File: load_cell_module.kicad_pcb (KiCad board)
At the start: 2 copper layers, 0 parts

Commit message: Finalized board shape
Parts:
- added H1: MountingScrew, MountingHole:MountingHole_3.2mm_M3, F.Cu at (144.0, 84.0)
- added H2: MountingScrew, MountingHole:MountingHole_3.2mm_M3, F.Cu at (176.0, 84.0)
- added H3: MountingScrew, MountingHole:MountingHole_3.2mm_M3, F.Cu at (144.0, 126.0)
- added H4: MountingScrew, MountingHole:MountingHole_3.2mm_M3, F.Cu at (176.0, 126.0)
- added U1: ~, integral0_lite:integral0_lite, F.Cu at (160.0, 80.7)
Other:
- board outline added: 40 x 50 mm

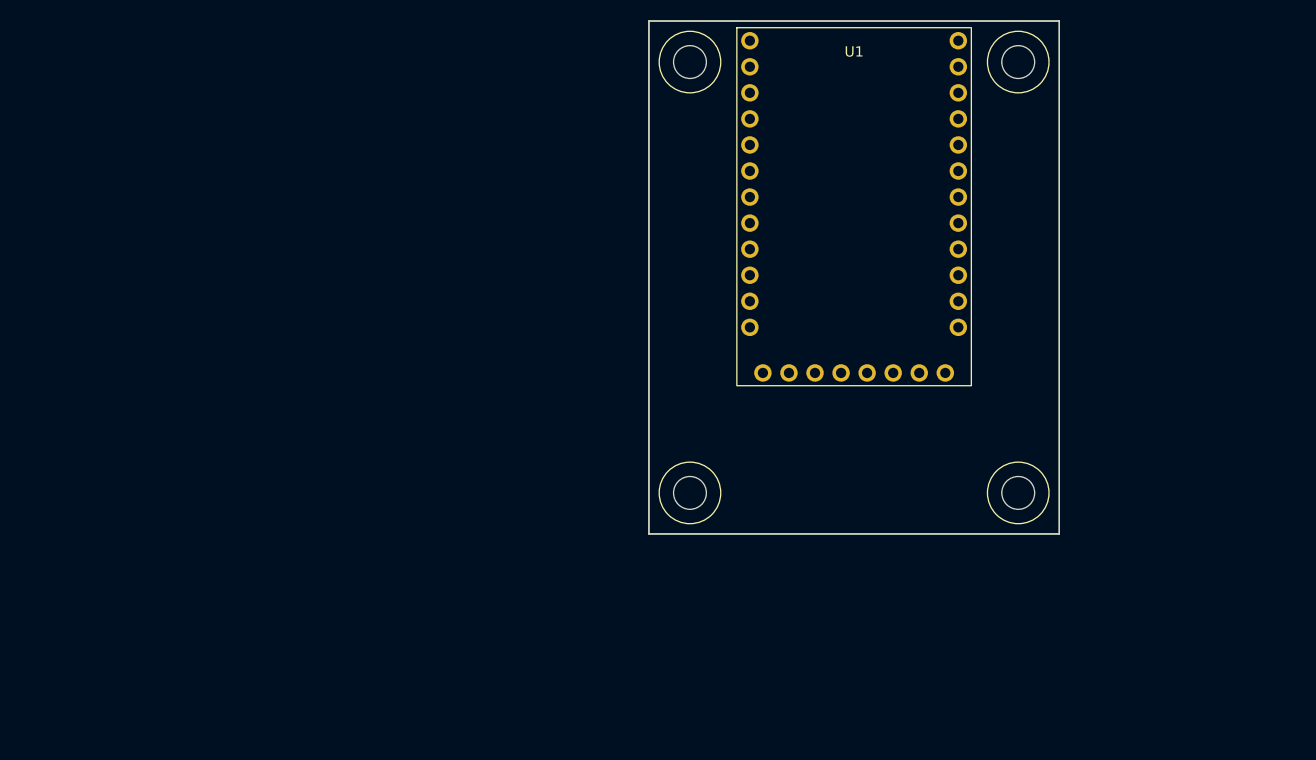
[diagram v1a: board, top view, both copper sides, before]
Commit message: Added side tab
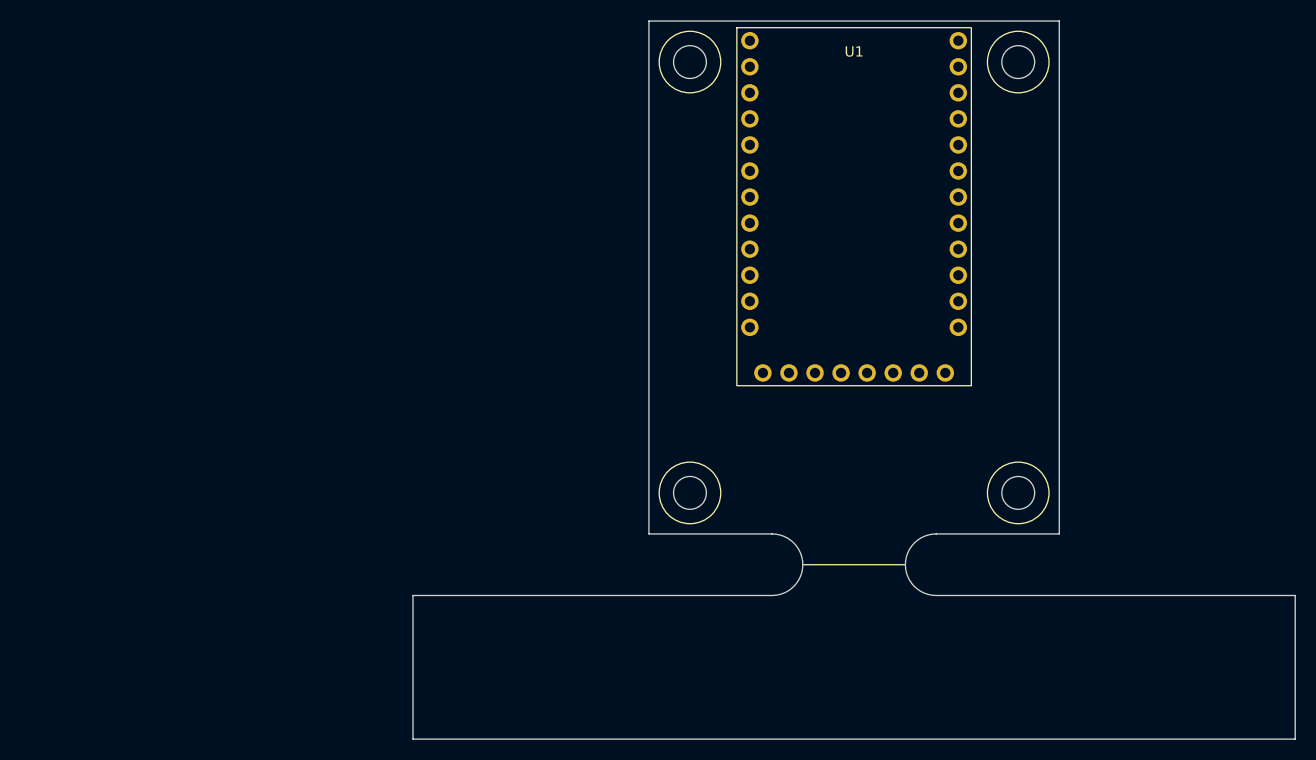
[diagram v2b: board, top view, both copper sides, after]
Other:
- board size 40 x 50 mm -> 86 x 70 mm
- board text added: "Copyright (C) 2026 Rowan Zhang"
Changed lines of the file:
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@@
 		)
+	)
+	(gr_circle
+		(center 144 84)
+		(end 144 87)
+		(stroke
+			(width 0.1)
+			(type default)
+		)
+		(fill no)
+		(layer "F.SilkS")
+	)
+	(gr_circle
+		(center 144 126)
+		(end 144 129)
+		(stroke
+			(width 0.1)
+			(type default)
+		)
+		(fill no)
+		(layer "F.SilkS")
+	)
+	(gr_line
+		(start 155 133)
+		(end 165 133)
+		(stroke
+			(width 0.1)
+			(type default)
+		)
+		(layer "F.SilkS")
+	)
+	(gr_circle
+		(center 176 84)
+		(end 176 87)
+		(stroke
+			(width 0.1)
+			(type default)
+		)
+		(fill no)
+		(layer "F.SilkS")
+	)
+	(gr_circle
+		(center 176 126)
+		(end 176 129)
+		(stroke
+			(width 0.1)
+			(type default)
+		)
+		(fill no)
+		(layer "F.SilkS")
+	)
+	(gr_line
+		(start 155 133)
+		(end 165 133)
+		(stroke
+			(width 0.1)
+			(type default)
+		)
+		(layer "B.SilkS")
+	)
+	(gr_rect
+		(start 117 136)
+		(end 203 150)
+		(stroke
+			(width 0.1)
+			(type solid)
+		)
+		(fill no)
+		(layer "Dwgs.User")
 	)
 	(gr_rect
@@
 		)
 		(fill no)
-		(layer "F.SilkS")
-	)
-	(gr_circle
-		(center 144 84)
-		(end 144 87)
-		(stroke
-			(width 0.1)
-			(type default)
-		)
-		(fill no)
-		(layer "F.SilkS")
-	)
-	(gr_circle
-		(center 144 126)
-		(end 144 129)
-		(stroke
-			(width 0.1)
-			(type default)
-		)
-		(fill no)
-		(layer "F.SilkS")
-	)
-	(gr_circle
-		(center 176 84)
-		(end 176 87)
-		(stroke
-			(width 0.1)
-			(type default)
-		)
-		(fill no)
-		(layer "F.SilkS")
-	)
-	(gr_circle
-		(center 176 126)
-		(end 176 129)
-		(stroke
-			(width 0.1)
-			(type default)
-		)
-		(fill no)
-		(layer "F.SilkS")
+		(layer "Dwgs.User")
+	)
+	(gr_arc
+		(start 152 130)
+		(mid 155 133)
+		(end 152 136)
+		(stroke
+			(width 0.1)
+			(type solid)
+		)
+		(layer "Dwgs.User")
 	)
 	(gr_rect
+		(start 155 130)
+		(end 165 136)
+		(stroke
+			(width 0.1)
+			(type solid)
+		)
+		(fill no)
+		(layer "Dwgs.User")
+	)
+	(gr_arc
+		(start 168 136)
+		(mid 165 133)
+		(end 168 130)
+		(stroke
+			(width 0.1)
+			(type solid)
+		)
+		(layer "Dwgs.User")
+	)
+	(gr_line
+		(start 117 136)
+		(end 152 136)
+		(stroke
+			(width 0.05)
+			(type default)
+		)
+		(layer "Edge.Cuts")
+	)
+	(gr_line
+		(start 117 150)
+		(end 117 136)
+		(stroke
+			(width 0.05)
+			(type default)
+		)
+		(layer "Edge.Cuts")
+	)
+	(gr_line
 		(start 140 80)
+		(end 180 80)
+		(stroke
+			(width 0.05)
+			(type default)
+		)
+		(layer "Edge.Cuts")
+	)
+	(gr_line
+		(start 140 130)
+		(end 140 80)
+		(stroke
+			(width 0.05)
+			(type default)
+		)
+		(layer "Edge.Cuts")
+	)
+	(gr_line
+		(start 152 130)
+		(end 140 130)
+		(stroke
+			(width 0.05)
+			(type default)
+		)
+		(layer "Edge.Cuts")
+	)
+	(gr_arc
+		(start 152 130)
+		(mid 155 133)
+		(end 152 136)
+		(stroke
+			(width 0.05)
+			(type default)
+		)
+		(layer "Edge.Cuts")
+	)
+	(gr_arc
+		(start 168 136)
+		(mid 165 133)
+		(end 168 130)
+		(stroke
+			(width 0.05)
+			(type default)
+		)
+		(layer "Edge.Cuts")
+	)
+	(gr_line
+		(start 168 136)
+		(end 203 136)
+		(stroke
+			(width 0.05)
+			(type default)
+		)
+		(layer "Edge.Cuts")
+	)
+	(gr_line
+		(start 180 80)
 		(end 180 130)
 		(stroke
@@
 			(type default)
 		)
-		(fill no)
-		(layer "Edge.Cuts")
+		(layer "Edge.Cuts")
+	)
+	(gr_line
+		(start 180 130)
+		(end 168 130)
+		(stroke
+			(width 0.05)
+			(type default)
+		)
+		(layer "Edge.Cuts")
+	)
+	(gr_line
+		(start 203 136)
+		(end 203 150)
+		(stroke
+			(width 0.05)
+			(type default)
+		)
+		(layer "Edge.Cuts")
+	)
+	(gr_line
+		(start 203 150)
+		(end 117 150)
+		(stroke
+			(width 0.05)
+			(type default)
+		)
+		(layer "Edge.Cuts")
+	)
+	(gr_text "Copyright (C) 2026 Rowan Zhang"
+		(at 160 82 0)
+		(layer "B.SilkS")
+		(effects
+			(font
+				(size 0.5 0.5)
+				(thickness 0.1)
+			)
+			(justify mirror)
+		)
 	)
 	(embedded_fonts no)

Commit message: Changed form factor
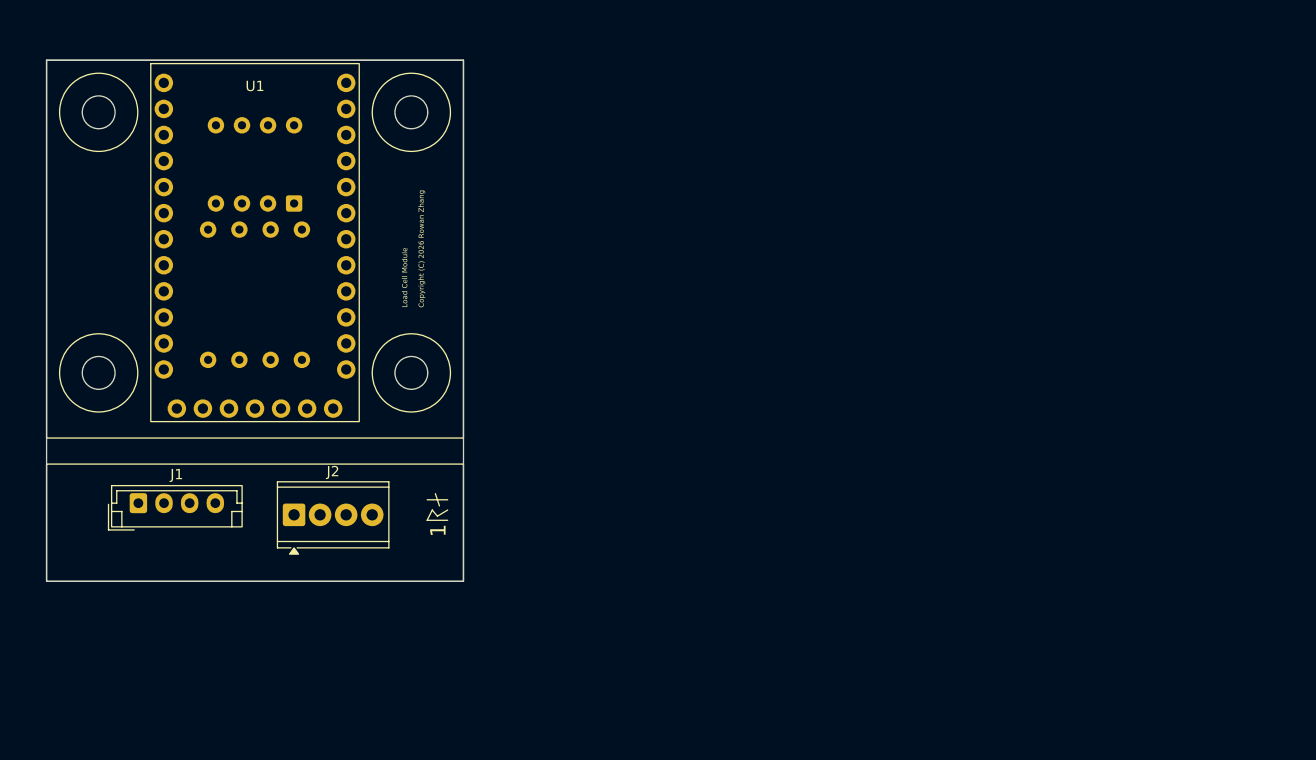
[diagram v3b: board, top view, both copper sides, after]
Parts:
- added J1: Conn_01x04, Connector_JST:JST_EH_B4B-EH-A_1x04_P2.50mm_Vertical, F.Cu at (90.2, 127.0)
- added J2: Screw_Terminal_01x04, TerminalBlock_Phoenix:TerminalBlock_Phoenix_MPT-0,5-4-2.54_1x04_P2.54mm_Horizontal, F.Cu at (105.4, 128.1)
- added R1: 100k, resistor:R_Axial_DIN0207_L6.3mm_D2.5mm_P7.62mm_Horizontal, B.Cu at (106.2, 100.3)
- added R2: 100k, resistor:R_Axial_DIN0207_L6.3mm_D2.5mm_P7.62mm_Horizontal, B.Cu at (103.1, 113.0)
- added R3: 100k, resistor:R_Axial_DIN0207_L6.3mm_D2.5mm_P7.62mm_Horizontal, B.Cu at (100.1, 113.0)
- added R4: 100k, resistor:R_Axial_DIN0207_L6.3mm_D2.5mm_P7.62mm_Horizontal, B.Cu at (97.0, 113.0)
- added U2: RC4558, Package_DIP:DIP-8_W7.62mm, B.Cu at (105.4, 97.8)
- U1: footprint integral0_lite:integral0_lite -> laplace0_lite:laplace0_lite
- moved H4 60.3 mm to (116.8, 114.3)
- moved H2 59.4 mm to (116.8, 88.9), turned to 0 degrees
- moved H3 58.8 mm to (86.4, 114.3)
- moved U1 58.6 mm to (101.6, 86.0)
- moved H1 57.8 mm to (86.4, 88.9), turned to 0 degrees
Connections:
- U1 pad 1: unconnected-(U1-+24-Pad1) -> +5V
- U1 pad 2: unconnected-(U1-+5-Pad2) -> +3V3
- U1 pad 20: unconnected-(U1-PC1-Pad20) -> GND
- U1 pad 7: unconnected-(U1-GHS2-Pad7) -> PA6
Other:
- board size 86 x 70 mm -> 40.6 x 50.8 mm
- board text added: "1"
- board text added: "Load Cell Module Copyright (C) 2026 Rowan Zhang"
- board text removed: "Copyright (C) 2026 Rowan Zhang"

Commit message: Finished PCB
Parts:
- moved J1 5.41 mm to (90.2, 132.4)
- moved J2 3.30 mm to (105.4, 131.4)
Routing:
- net +5V: track 0.00 -> 68.2 mm
- net WHITE: track 0.00 -> 55.7 mm, vias 0 -> 1
- net GREEN: track 0.00 -> 55.1 mm
- net Net-(R1-Pad1): track 0.00 -> 18.1 mm
- net PA6: track 0.00 -> 16.6 mm
- net GND: vias 0 -> 42
- added copper zone on B.Cu, net GND
- added copper zone on F.Cu, net GND
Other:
- board size 40.6 x 50.8 mm -> 40.6 x 52.1 mm
- board text added: "+5v GND WHI GRE"
- board text added: "+5v GND WHITE GREEN"

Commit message: Changed resistor values
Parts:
- R1, R2: value 100k -> 10k
- R3, R4: value 100k -> 1Meg
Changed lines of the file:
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@@
 		(capping no)
 		(filling no)
-		(zone_defaults)
 		(pcbplotparams
 			(layerselection 0x00000000_00000000_55555555_5755f5ff)
@@
 			)
 		)
-		(property "Value" "100k"
+		(property "Value" "1Meg"
 			(at 6.35 0 90)
 			(layer "B.SilkS")
@@
 			)
 		)
-		(property "Value" "100k"
+		(property "Value" "1Meg"
 			(at 6.35 0 90)
 			(layer "B.SilkS")
@@
 			)
 		)
-		(property "Value" "100k"
+		(property "Value" "10k"
 			(at 6.35 0 90)
 			(layer "B.SilkS")
@@
 			)
 		)
-		(property "Value" "100k"
+		(property "Value" "10k"
 			(at 6.35 0 90)
 			(layer "B.SilkS")

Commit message: Added version number
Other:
- board text added: "v1.0"
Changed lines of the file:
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@@
+		)
+	)
+	(gr_text "v1.0"
+		(at 86.36 101.6 270)
+		(layer "F.SilkS")
+		(effects
+			(font
+				(size 1 1)
+				(thickness 0.1)
+			)
 		)
 	)
